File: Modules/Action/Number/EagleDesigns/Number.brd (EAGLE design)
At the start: 100 x 80 mm, 7 parts, among them U2 ATMEGA328P_TQFP

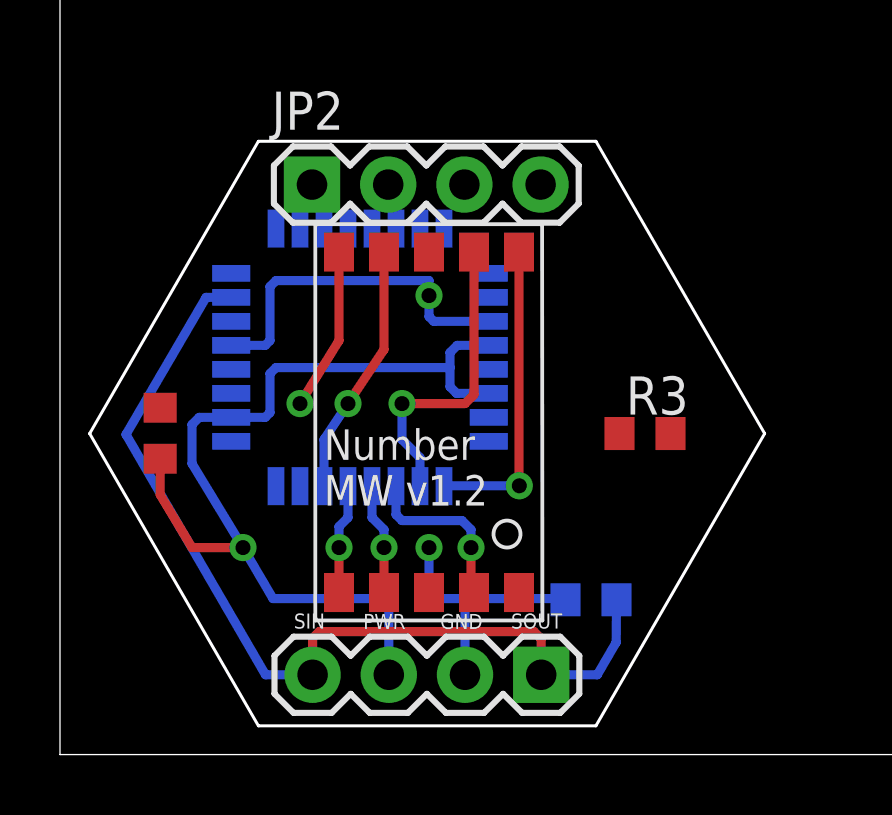
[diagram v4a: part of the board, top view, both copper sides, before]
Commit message: Number: removed crystal, modified for new bootloader #49
also added resistor to make sure that we address #49
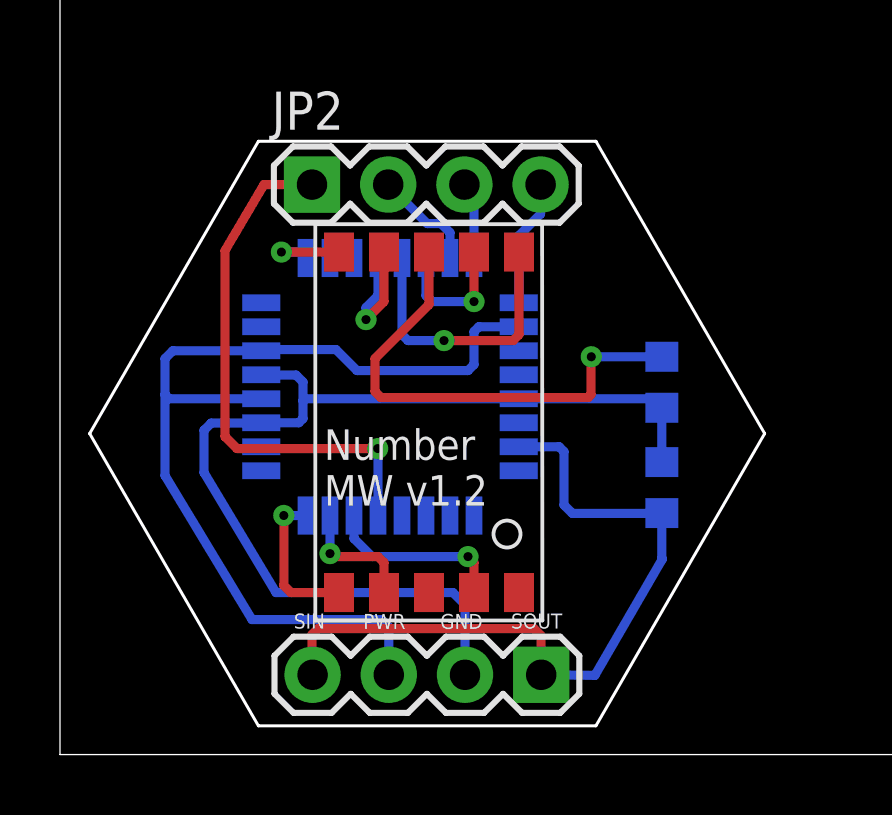
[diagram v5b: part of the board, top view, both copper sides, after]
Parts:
- removed R2: 10K, resistor:R0603
- moved R1 4.42 mm to (20.1, 8.90), turned to 270 degrees
- moved R3 1.80 mm to (20.1, 12.4), flipped to the bottom, turned to 90 degrees
- moved U2 1.40 mm to (11.0, 12.3), turned to 180 degrees
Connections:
- net 7SEG-G/MOSI renamed MOSI
- removed net RX: U2.30
- removed net TX: U2.31
- net 7SEG-A: now also U2.14; no longer U2.10
- net 7SEG-B: now also U2.13; no longer U2.9
- net 7SEG-C: now also U2.30; no longer U2.11
- net 7SEG-D: now also U2.31; no longer U2.12
- net 7SEG-E: now also U2.32; no longer U2.13
- net 7SEG-F: now also U2.12; no longer U2.14
- net 7SEG-G: now also U2.9
- net RESET: no longer R2.1
- net VCC: no longer R2.2
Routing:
- net RESET: track 0.00 -> 17.8 mm, vias 0 -> 1
- net N$1: track 0.00 -> 16.3 mm, vias 0 -> 1
- net GND: track 20.5 -> 35.0 mm, vias 2 -> 0
- net 1X3SIN-SOUT: track 31.7 -> 25.0 mm
- net 7SEG-A: track 10.3 -> 4.59 mm
- net SCK: track 0.00 -> 4.24 mm
- net 7SEG-F: track 8.41 -> 4.72 mm
- net MOSI: track 0.00 -> 3.57 mm
- net MISO: track 0.00 -> 2.58 mm
- net 7SEG-G: track 5.42 -> 2.92 mm
- net 7SEG-E: track 3.67 -> 5.01 mm
- net 7SEG-B: track 10.3 -> 9.37 mm
- net VCC: track 31.9 -> 32.5 mm, vias 1 -> 0
